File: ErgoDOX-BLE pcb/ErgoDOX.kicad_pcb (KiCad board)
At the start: 2 copper layers, 182.8 x 158.9 mm, 118 parts, among them J1 Conn_01x04, J2 Conn_01x02_Female, J3 Conn_01x02_Female, J4 Conn_01x02, J5 Conn_01x02, J6 6PIN, P1 USB_C_Plug_USB2.0, Q1 Q_NPN_BCE, SW0:10 SW0:3, SW0:11 SW0:2, SW0:12 SW0:1, SW0:7 SW0:6, SW0:8 SW0:5, SW0:9 SW0:4, SW1:10 SW1:3, SW1:11 SW1:2, SW1:12 SW1:1, SW1:13 SW1:0, SW1:9 SW1:4, SW2:10 SW2:3, SW2:11 SW2:2, SW2:12 SW2:1, SW2:13 SW2:0, SW2:7 SW2:6, SW2:8 SW2:5, SW2:9 SW2:4, SW3:10 SW3:3, SW3:11 SW3:2, SW3:12 SW3:1, SW3:13 SW3:0, SW3:8 SW3:5, SW3:9 SW3:4, SW4:10 SW4:3, SW4:11 SW4:2, SW4:12 SW4:1, SW4:13 SW4:0, SW4:7 SW4:6, SW4:8 SW4:5, SW4:9 SW4:4, SW5:10 SW5:3, SW5:11 SW5:2, SW5:12 SW5:1, SW5:13 SW5:0, SW5:7 SW5:6, SW5:8 SW5:5, SW5:9 SW5:4, U1 MCP23018, U3 C0720B001F

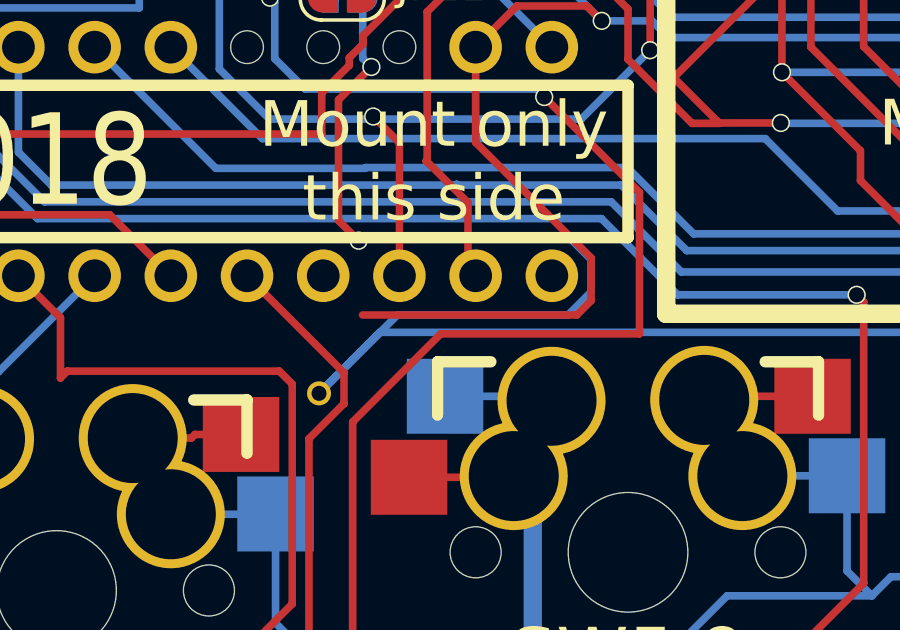
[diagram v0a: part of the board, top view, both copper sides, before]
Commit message: Begin playing around with replacing the 23018 with a 23017
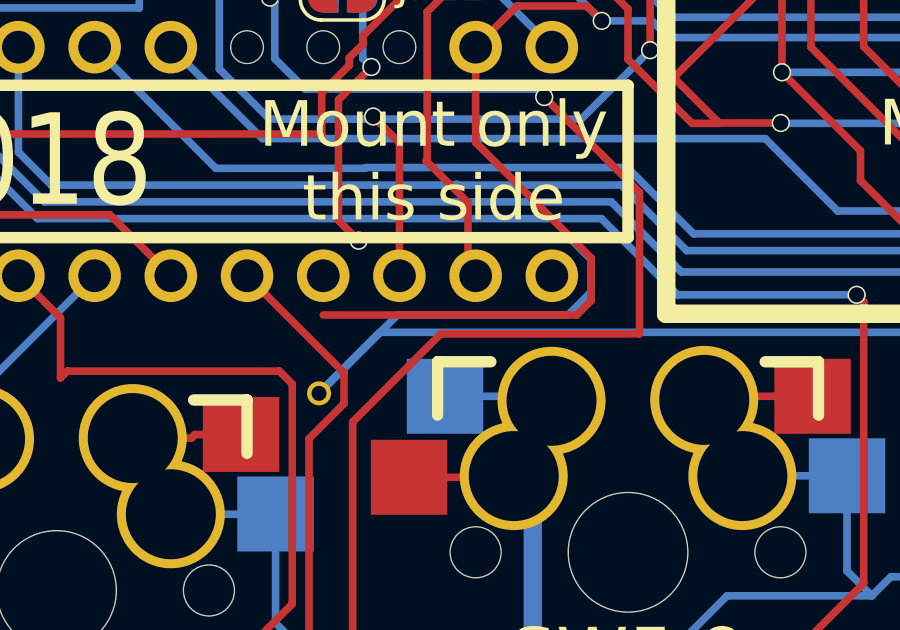
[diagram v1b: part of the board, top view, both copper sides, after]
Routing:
- net +3V3: track 334.2 -> 335.5 mm
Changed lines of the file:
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@@
   (segment (start 80.193202 42.601202) (end 82.140211 42.601202) (width 0.254) (layer "F.Cu") (net 61))
   (segment (start 92.940598 40.141447) (end 94.431376 38.650669) (width 0.254) (layer "F.Cu") (net 61))
+  (segment (start 105.41 50.165) (end 109.2581 54.0131) (width 0.254) (layer "F.Cu") (net 61))
+  (segment (start 109.2581 54.0131) (end 109.2581 55.44096) (width 0.254) (layer "F.Cu") (net 61))
   (segment (start 149.86 50.8) (end 154.305 50.8) (width 0.254) (layer "F.Cu") (net 61))
   (segment (start 105.41 46.99) (end 106.7816 45.6184) (width 0.254) (layer "F.Cu") (net 61))
   (segment (start 157.988 91.821) (end 157.988 60.198) (width 0.254) (layer "F.Cu") (net 61))
-  (segment (start 105.41 46.99) (end 105.41 50.165) (width 0.254) (layer "F.Cu") (net 61))
+  (segment (start 108.78096 55.9181) (end 100.33 55.9181) (width 0.254) (layer "F.Cu") (net 61))
+  (segment (start 109.2581 55.44096) (end 108.78096 55.9181) (width 0.254) (layer "F.Cu") (net 61))
   (segment (start 106.7816 45.6184) (end 109.1184 45.6184) (width 0.254) (layer "F.Cu") (net 61))
   (segment (start 125.168931 46.863) (end 141.986 46.863) (width 0.254) (layer "F.Cu") (net 61))
-  (segment (start 109.2581 55.44096) (end 108.78096 55.9181) (width 0.254) (layer "F.Cu") (net 61))
-  (segment (start 108.78096 55.9181) (end 101.6381 55.9181) (width 0.254) (layer "F.Cu") (net 61))
+  (segment (start 105.41 46.99) (end 105.41 50.165) (width 0.254) (layer "F.Cu") (net 61))
   (segment (start 124.975831 46.6699) (end 125.168931 46.863) (width 0.254) (layer "F.Cu") (net 61))
   (segment (start 103.087898 42.327102) (end 107.405898 42.327102) (width 0.254) (layer "F.Cu") (net 61))
   (segment (start 99.411465 38.650669) (end 103.087898 42.327102) (width 0.254) (layer "F.Cu") (net 61))
   (segment (start 157.988 60.198) (end 160.5475 60.198) (width 0.254) (layer "F.Cu") (net 61))
-  (segment (start 105.41 50.165) (end 109.2581 54.0131) (width 0.254) (layer "F.Cu") (net 61))
   (segment (start 141.986 46.863) (end 142.621 46.228) (width 0.254) (layer "F.Cu") (net 61))
   (segment (start 154.305 50.8) (end 157.505647 54.000647) (width 0.254) (layer "F.Cu") (net 61))
   (segment (start 78.456 40.864) (end 80.193202 42.601202) (width 0.254) (layer "F.Cu") (net 61))
   (segment (start 92.940598 42.436431) (end 92.940598 40.141447) (width 0.254) (layer "F.Cu") (net 61))
-  (segment (start 109.2581 54.0131) (end 109.2581 55.44096) (width 0.254) (layer "F.Cu") (net 61))
   (segment (start 89.651798 44.387499) (end 90.98953 44.387499) (width 0.254) (layer "F.Cu") (net 61))
   (segment (start 157.505647 54.000647) (end 157.530724 54.000647) (width 0.254) (layer "F.Cu") (net 61))

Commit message: A lot of footprint work
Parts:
- added ?: , clipboard:e88a871c-9447-4417-8450-794959ff4df0, B.Cu at (63.5, 134.0)
- C1: footprint Capacitor_THT:C_Axial_L5.1mm_D3.1mm_P7.50mm_Horizontal -> Capacitor_THT:CP_Radial_Tantal_D5.0mm_P5.00mm
- moved C1 3.28 mm to (63.5, 135.5)
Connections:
- U1 pad 11: VCC -> +3V3
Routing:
- net Net-(C1-Pad2): track 10.4 -> 16.4 mm
- net /COL6: track 177.1 -> 178.2 mm
- net +3V3: track 335.5 -> 336.6 mm
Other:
- board text added: "C1"

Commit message: Routing everything
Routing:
- net /COL3: track 247.5 -> 250.8 mm
- net /COL2: track 291.5 -> 293.3 mm
- net /ROW0: track 293.6 -> 292.3 mm
- net /COL6: track 178.2 -> 177.3 mm
- net /COL1: track 357.7 -> 358.4 mm

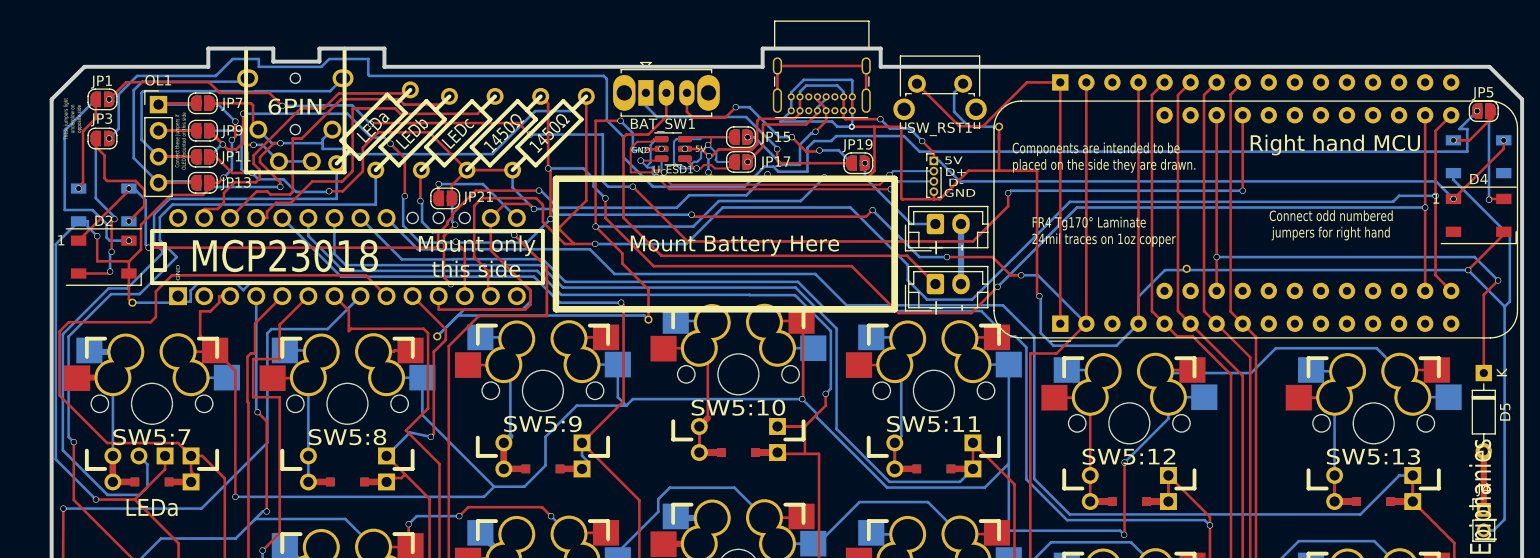
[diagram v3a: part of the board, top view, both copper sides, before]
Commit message: Move my bank of resistors because they overlapped with another footprint
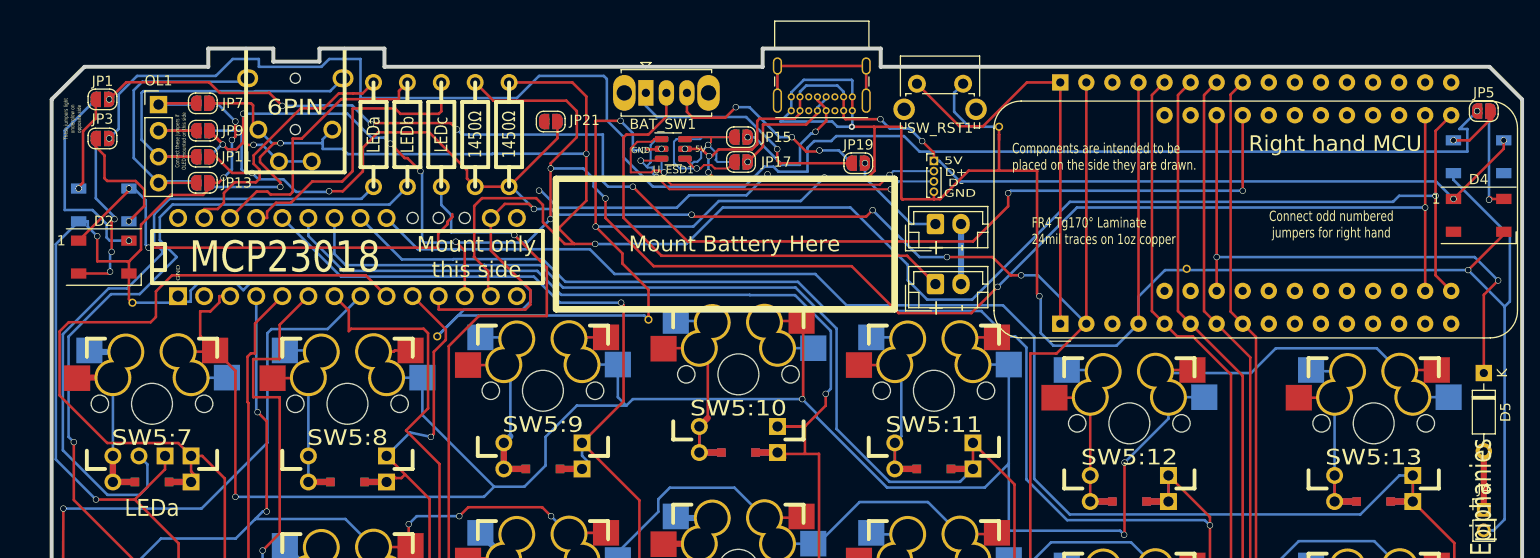
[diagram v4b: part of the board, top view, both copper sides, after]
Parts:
- moved JP21 12.7 mm to (111.3, 37.6)
- moved JP22 12.7 mm to (111.3, 37.6)
- moved R1 3.94 mm to (107.2, 38.9), turned to 90 degrees
- moved R2 2.80 mm to (103.9, 38.9), turned to 90 degrees
- moved RC1 1.66 mm to (100.6, 38.9), turned to -90 degrees
- moved RA1 0.76 mm to (94.0, 38.9), turned to -90 degrees
- moved RB1 0.52 mm to (97.3, 38.9), turned to -90 degrees
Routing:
- net /MCP23018_ADDR_Selector: track 11.8 -> 0.00 mm, vias 1 -> 0
- net /SCL: track 190.0 -> 199.8 mm
- net +5V: track 181.8 -> 172.4 mm
- net GND: track 699.2 -> 690.0 mm, vias 18 -> 16
- net /SDA: track 207.5 -> 213.4 mm, vias 4 -> 5
- net +3V3: track 336.2 -> 340.4 mm
- net Net-(LED_C1-Pad1): track 114.1 -> 110.5 mm, vias 2 -> 1
- net /LED_B: track 30.0 -> 26.5 mm
- net /LED_A: track 28.5 -> 25.2 mm
- net Net-(JP3-Pad2): track 158.1 -> 161.2 mm
- net /LED_C: track 32.6 -> 29.5 mm
- net Net-(LED_A1-Pad1): track 64.0 -> 64.7 mm

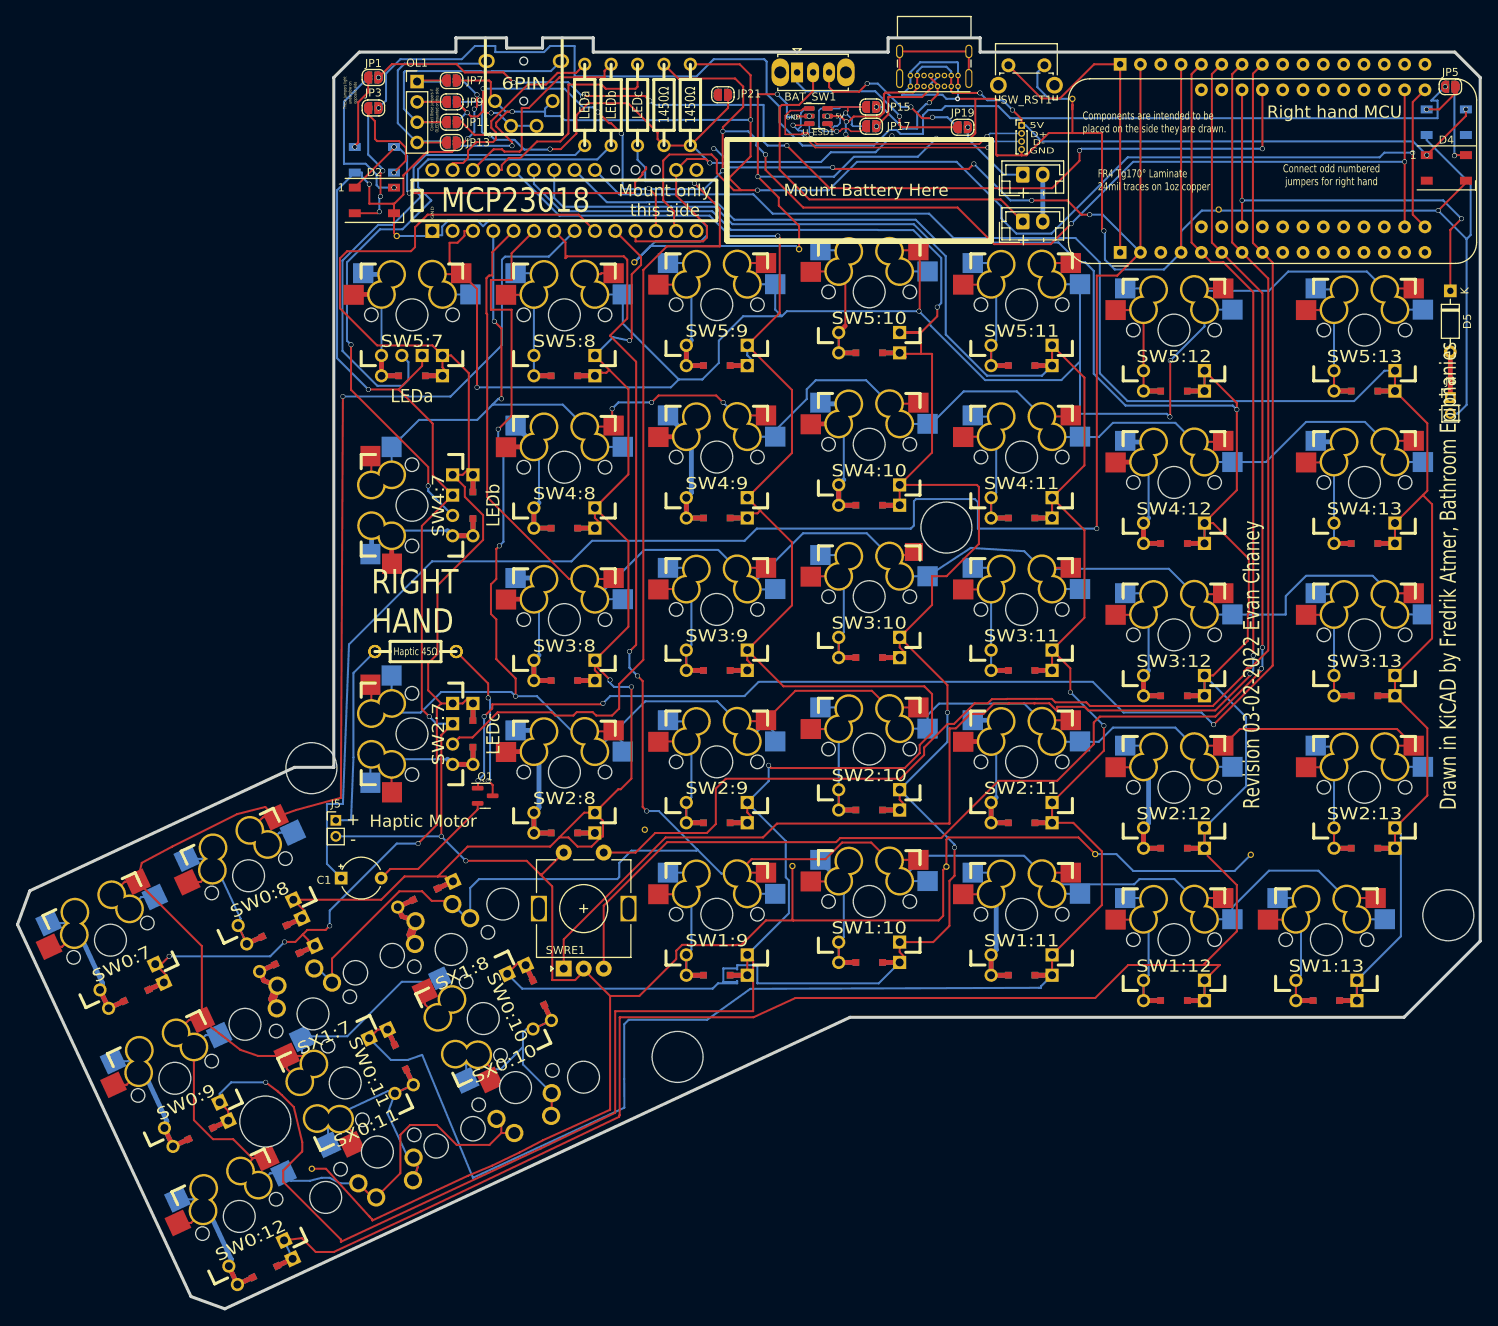
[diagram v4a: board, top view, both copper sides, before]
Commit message: Ground fills for everyone
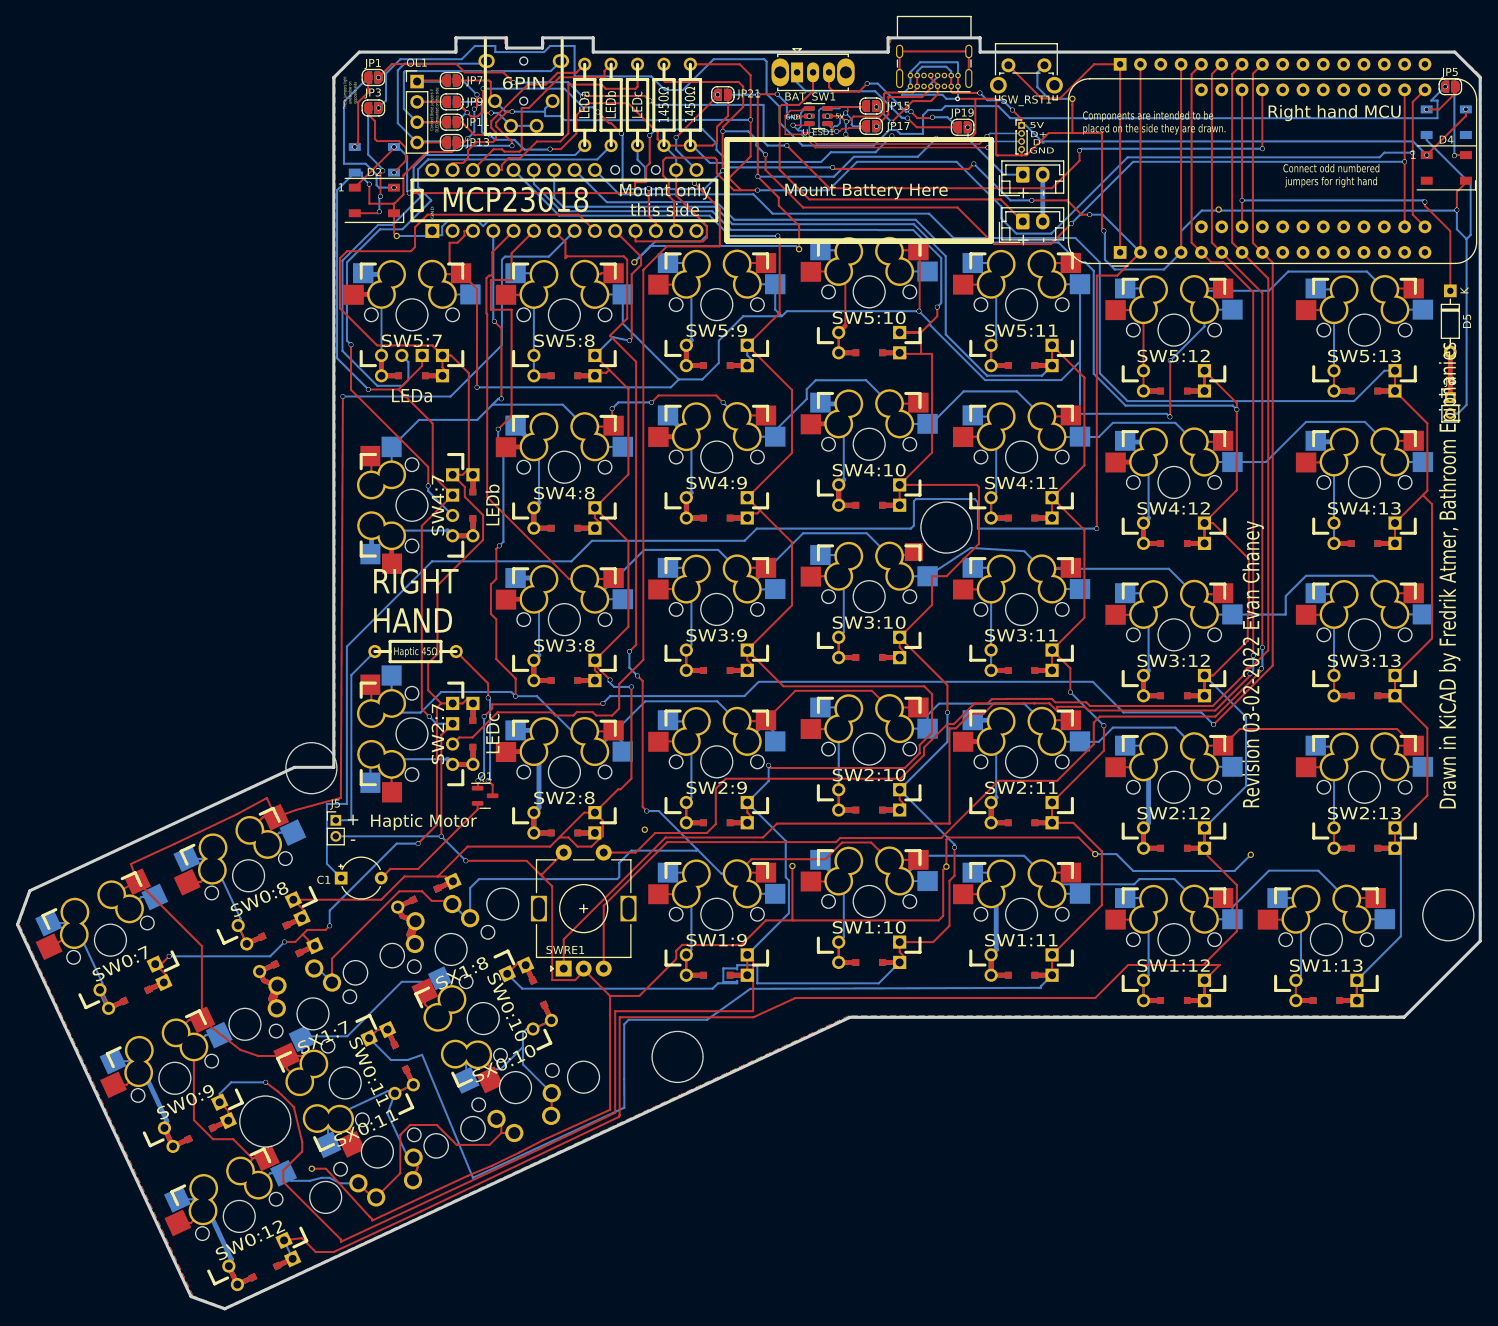
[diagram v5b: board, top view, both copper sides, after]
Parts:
- removed the R3 at (72.8, 107.2)
- moved JP15 0.12 mm to (129.8, 39.0)
- moved JP16 0.12 mm to (129.8, 39.0)
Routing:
- net +5V: track 172.4 -> 187.1 mm
- net /MCP23018_ADDR_Selector: track 0.00 -> 12.6 mm, vias 0 -> 2
- net GND: track 690.0 -> 693.4 mm, vias 16 -> 17
- net /WirelessCharger: track 55.1 -> 52.5 mm
- net /ROW0: track 292.3 -> 294.7 mm
- net /D_IN_RIGHT+: track 14.2 -> 12.4 mm
- net Net-(JP3-Pad2): track 161.2 -> 162.6 mm
- net /SCL: track 199.8 -> 201.0 mm
- net +3V3: track 340.4 -> 341.3 mm, vias 8 -> 7
- net Net-(BAT_SW1-Pad1): track 24.3 -> 23.6 mm
- added copper zone on B.Cu, net GND
- added copper zone on F.Cu, net GND
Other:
- board text added: "Haptic 45Ω"
- board text removed: "FR4 Tg170° Laminate 24mil traces on 1oz copper"
